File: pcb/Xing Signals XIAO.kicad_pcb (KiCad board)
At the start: 2 copper layers, 59.1 x 45.7 mm, 48 parts, among them J1 Barrel_Jack_Switch, J10 Signals, J2 DCC IN, J3 Signals, J4 Signal Gate 1, J5 Signal Gate 2, J6 Conn_01x07_Pin, J7 Sensor Power, J8 Screw_Terminal_01x04, J9 Conn_01x07_Pin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

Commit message: Version 1.1 of the PCB
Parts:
- removed J5: Signal Gate 2, Connector_PinHeader_2.54mm:PinHeader_1x03_P2.54mm_Vertical
- removed R16, R17: 100, Resistor_SMD:R_0402_1005Metric
- added R18: 100, Resistor_SMD:R_0402_1005Metric, F.Cu at (60.5, 63.2)
- added R19: 100, Resistor_SMD:R_0402_1005Metric, F.Cu at (60.5, 60.5)
- added R20: 100, Resistor_SMD:R_0402_1005Metric, F.Cu at (60.5, 68.3)
- J4: value Signal Gate 1 -> Conn_02x03_Top_Bottom; footprint Connector_PinHeader_2.54mm:PinHeader_1x03_P2.54mm_Vertical -> Connector_PinHeader_2.54mm:PinHeader_2x03_P2.54mm_Vertical
- R1: value 100ohm -> 100; footprint Resistor_SMD:R_1206_3216Metric -> Resistor_SMD:R_0402_1005Metric
- R2: value 100ohm -> 1k
- R3: value 200 -> 1k
- moved J7 14.8 mm to (64.5, 77.2)
- moved D7 9.70 mm to (84.1, 77.4), turned to -90 degrees
- moved R2 8.98 mm to (77.7, 62.2)
- moved J3 8.95 mm to (75.2, 77.2)
- moved D6 8.18 mm to (71.4, 77.4), turned to -90 degrees
- moved Q2 4.59 mm to (70.9, 68.2)
- moved R4 4.59 mm to (71.8, 64.8)
- moved BR1 4.38 mm to (86.4, 66.4)
- moved VIN 4.32 mm to (88.9, 57.9)
- moved C1 3.82 mm to (96.2, 58.9)
- moved GND 3.78 mm to (83.8, 57.9)
- moved Q3 3.34 mm to (74.7, 68.2)
- moved R1 3.31 mm to (60.5, 65.8), turned to 180 degrees
- moved R5 3.26 mm to (75.6, 64.8)
- moved J4 2.81 mm to (51.1, 49.3)
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- renumbered TP3 to +5V, TP1 to GND, TP2 to VIN
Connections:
- D1 pad 1: GND -> Net-(D1-K)
- D2 pad 1: GND -> Net-(D2-K)
- D3 pad 1: GND -> Net-(D3-K)
- D4 pad 1: GND -> Net-(D4-K)
- D6 pad 1: GND -> Net-(D6-K)
- D7 pad 1: GND -> Net-(D7-K)
- D7 pad 2: Net-(D7-A) -> Net-(D6-A)
- J3 pad 1: Net-(J3-Pin_1) -> Net-(D6-K)
- J3 pad 2: Net-(J3-Pin_2) -> Net-(D6-A)
- J3 pad 3: Net-(J3-Pin_3) -> Net-(D7-K)
- J4 pad 2: +3V3 -> GND
- J4 pad 3: GATE1 -> +3V3
- Q2 pad 2: Net-(Q2-E) -> GND
- Q2 pad 3: Net-(J3-Pin_1) -> Net-(D6-K)
- Q3 pad 2: Net-(Q3-E) -> GND
- Q3 pad 3: Net-(J3-Pin_3) -> Net-(D7-K)
- Q4 pad 3: Net-(Q4-C) -> +3V3
- Q5 pad 3: Net-(Q4-C) -> +3V3
- Q6 pad 3: Net-(Q4-C) -> +3V3
- Q7 pad 3: Net-(Q4-C) -> +3V3
- R1 pad 1: +3V3 -> GND
- R1 pad 2: Net-(Q4-C) -> Net-(D3-K)
- R2 pad 2: Net-(J3-Pin_2) -> Net-(D6-A)
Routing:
- net Net-(D6-A): track 1.80 -> 28.3 mm
- net Net-(Q4-C): track 20.8 -> 0.00 mm
- net Net-(D7-K): track 0.00 -> 15.8 mm, vias 0 -> 2
- net Net-(J3-Pin_2): track 14.1 -> 0.00 mm
- net Net-(D6-K): track 0.00 -> 14.0 mm
- net +3V3: track 115.3 -> 125.0 mm
- net Net-(Q3-E): track 9.72 -> 0.00 mm, vias 2 -> 0
- net Net-(J3-Pin_3): track 6.48 -> 0.00 mm
- net Net-(J3-Pin_1): track 6.48 -> 0.00 mm
- net Net-(Q2-E): track 6.13 -> 0.00 mm
- net Net-(U2-VI): track 38.9 -> 44.5 mm
- net SIGRIGHT: track 16.3 -> 12.7 mm
- net Net-(J2-Pin_2): track 19.8 -> 16.5 mm
- net Net-(BR1-~.): track 13.0 -> 10.4 mm
- net Net-(D7-A): track 1.82 -> 0.00 mm
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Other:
- board text added: "Crossing Gate Control Version 1.1 (C) Peter Buelow Februrary 2024"
- board text removed: "Crossing Gate Control Version 1.0 (C) Peter Buelow January 2024"

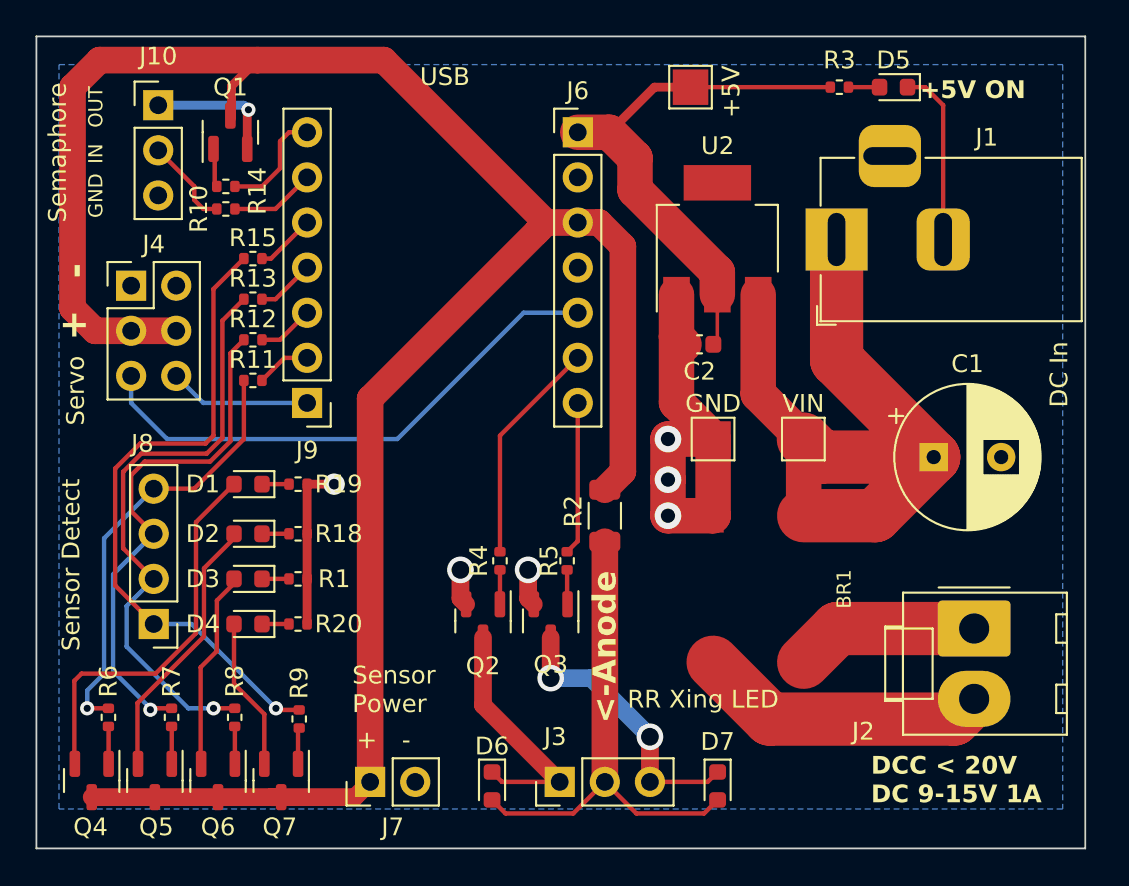
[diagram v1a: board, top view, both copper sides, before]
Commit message: Fixes to Version 1.1
* Trace fixups
* Components moved to better fit
* Move the sensor screw terminals next to each other
* Cleaned up the transistor layout for the sensor LED indicators
* Servo pins are now 2x3
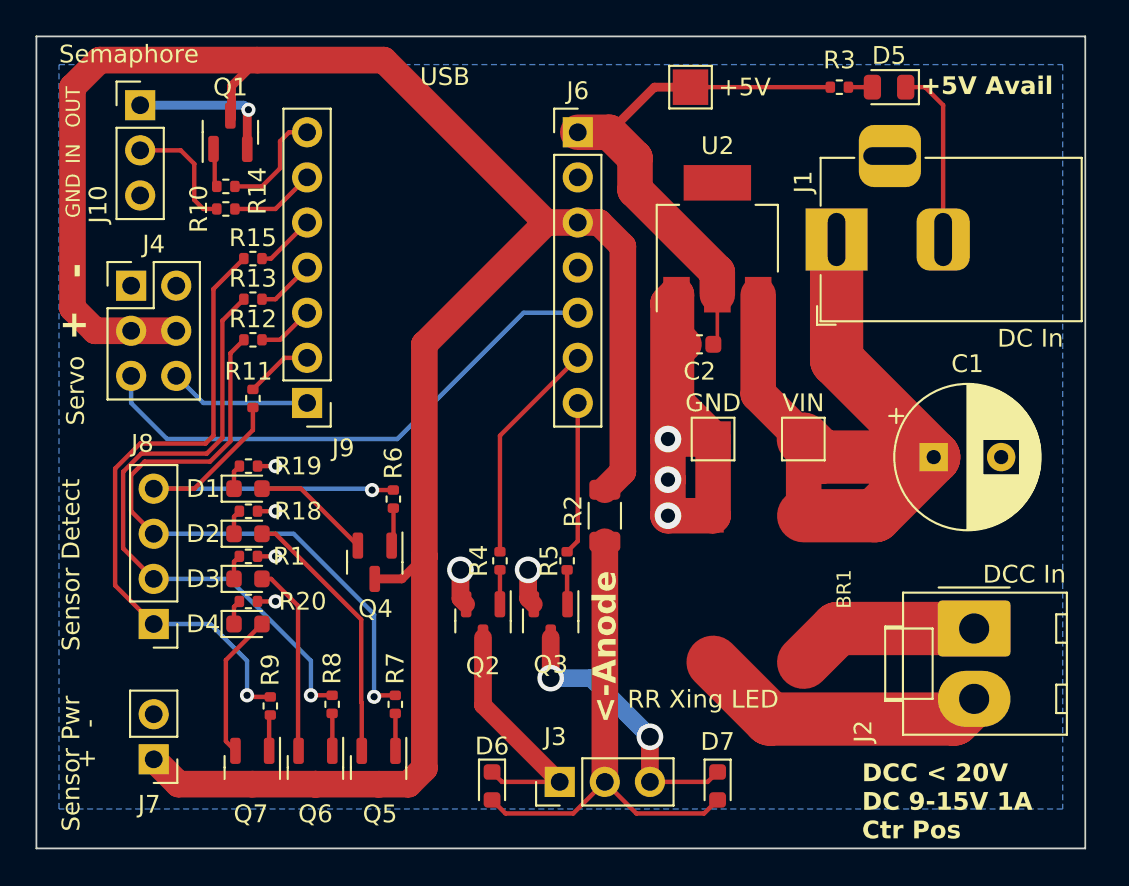
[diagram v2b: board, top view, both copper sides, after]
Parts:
- D5: value White -> Green; footprint LED_SMD:LED_0603_1608Metric -> LED_SMD:LED_0805_2012Metric
- J2: value DCC IN -> DCC In
- TP2: renamed from VIN; value +12V -> VIN
- moved R6 20.2 mm to (65.8, 61.3)
- moved Q4 20.1 mm to (64.8, 64.8)
- moved R7 12.6 mm to (65.9, 72.9)
- moved Q5 12.6 mm to (65.0, 76.4)
- moved J7 12.3 mm to (52.3, 75.9), turned to 180 degrees
- moved Q6 5.53 mm to (61.4, 76.4)
- moved R8 5.53 mm to (62.4, 72.8)
- moved R1 3.07 mm to (57.7, 64.5)
- moved R18 3.07 mm to (57.7, 62.0)
- moved R20 3.07 mm to (57.7, 67.1)
- moved R19 2.97 mm to (57.7, 59.4)
- moved Q7 1.78 mm to (57.9, 76.4)
- moved R9 1.78 mm to (58.9, 72.9)
- moved J10 1.02 mm to (51.6, 39.1)
- moved R11 1.02 mm to (57.9, 55.6), turned to 90 degrees
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- renumbered GND to TP1, +5V to TP3
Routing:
- net Net-(D1-A): track 21.9 -> 6.77 mm
- net DETECT2: track 29.1 -> 36.4 mm
- net GND: track 47.2 -> 50.3 mm, vias 6 -> 9
- net DETECT1: track 24.7 -> 21.7 mm
- net DETECT3: track 33.4 -> 35.3 mm
- net Net-(J10-Pin_2): track 5.11 -> 6.87 mm
- net Net-(J10-Pin_1): track 7.42 -> 8.44 mm
- net +3V3: track 125.0 -> 125.9 mm
- net DETECT4: track 36.8 -> 36.0 mm
- net Net-(J9-Pin_2): track 3.07 -> 3.79 mm
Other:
- board text added: "+5V Avail"
- board text added: "DCC < 20V DC 9-15V 1A Ctr Pos"
- board text added: "Sensor Pwr"
- board text removed: "+5V ON"
- board text removed: "DCC < 20V DC 9-15V 1A"
- board text removed: "Sensor Power"

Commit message: More fixes, ordered V1.1
* Added C3 to buffer the Servo current draw
* More fixes for traces
* Fixed TP2 to be VIN, not +12V
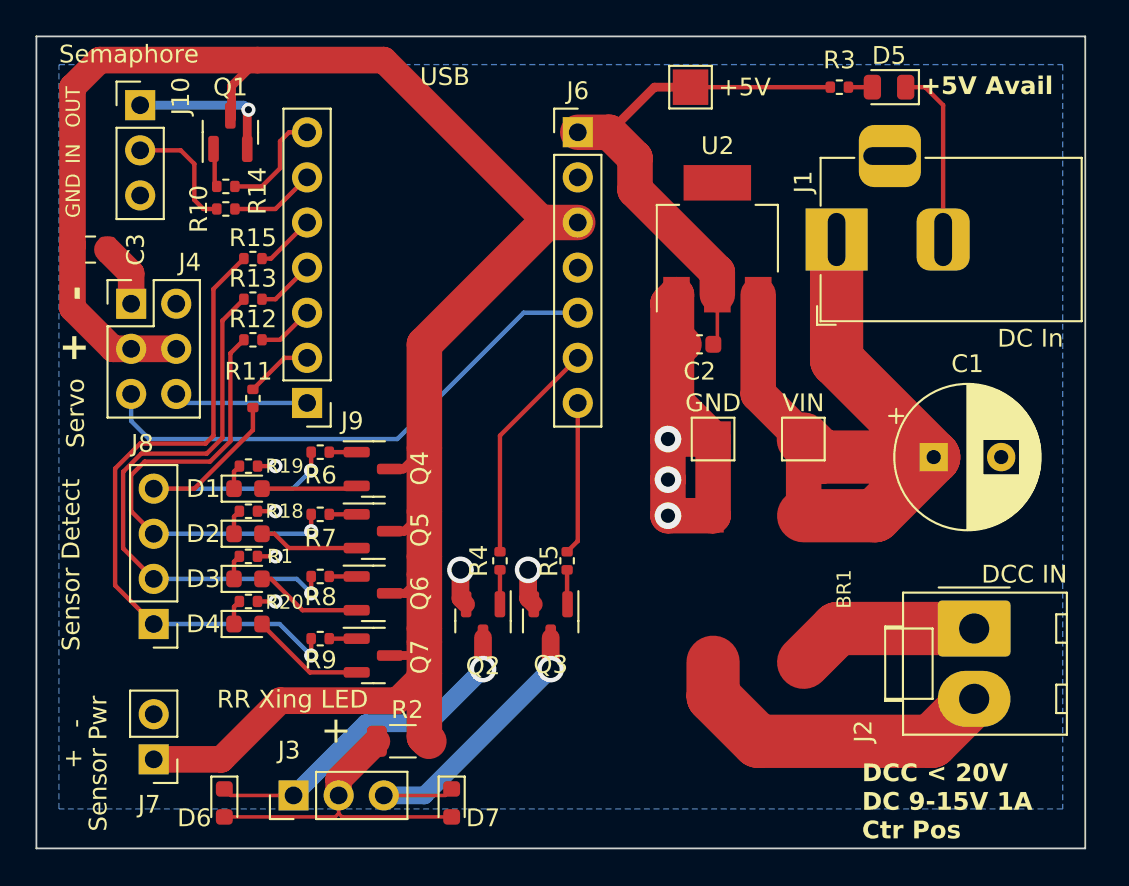
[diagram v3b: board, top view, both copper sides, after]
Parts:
- added C3: 47uf, Capacitor_SMD:C_0805_2012Metric, F.Cu at (48.8, 47.2)
- J2: value DCC In -> DCC IN
- moved R2 17.0 mm to (66.4, 74.9), turned to 180 degrees
- moved D6 15.1 mm to (56.3, 78.4)
- moved J3 15.0 mm to (60.2, 78.0)
- moved D7 15.0 mm to (69.1, 78.4)
- moved Q5 13.3 mm to (64.7, 63.1), turned to 0 degrees
- moved R7 11.5 mm to (61.7, 62.1), turned to 0 degrees
- moved Q6 10.3 mm to (64.7, 66.6), turned to 0 degrees
- moved Q7 9.28 mm to (64.7, 70.1), turned to 0 degrees
- moved R8 7.23 mm to (61.7, 65.7), turned to 180 degrees
- moved Q4 5.25 mm to (64.7, 59.6), turned to 0 degrees
- moved R6 4.89 mm to (61.7, 58.6), turned to 180 degrees
- moved R9 4.72 mm to (61.7, 69.2), turned to 180 degrees
- moved J4 1.02 mm to (51.1, 50.3)
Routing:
- net +3V3: track 125.9 -> 114.9 mm
- net Net-(D6-A): track 28.3 -> 17.9 mm
- net DETECT2: track 36.4 -> 26.1 mm
- net Net-(D2-A): track 15.0 -> 5.67 mm
- net Net-(D6-K): track 14.0 -> 19.4 mm, vias 0 -> 1
- net Net-(D3-A): track 10.8 -> 6.06 mm
- net DETECT3: track 35.3 -> 31.6 mm
- net GND: track 50.3 -> 53.9 mm
- net DETECT1: track 21.7 -> 18.5 mm
- net Net-(D7-K): track 15.8 -> 18.1 mm, vias 2 -> 1
- net Net-(J2-Pin_2): track 16.5 -> 18.7 mm
- net Net-(D4-A): track 8.21 -> 6.48 mm
- net Net-(D1-A): track 6.77 -> 5.40 mm
- net DETECT4: track 36.0 -> 37.2 mm
- net Net-(Q4-B): track 2.11 -> 1.54 mm
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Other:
- board text removed: "<-Anode"

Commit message: Version 1.2
* Fixed a clearance issue between J3 and C2
* Moved D6 and D7 a bit closer to J3
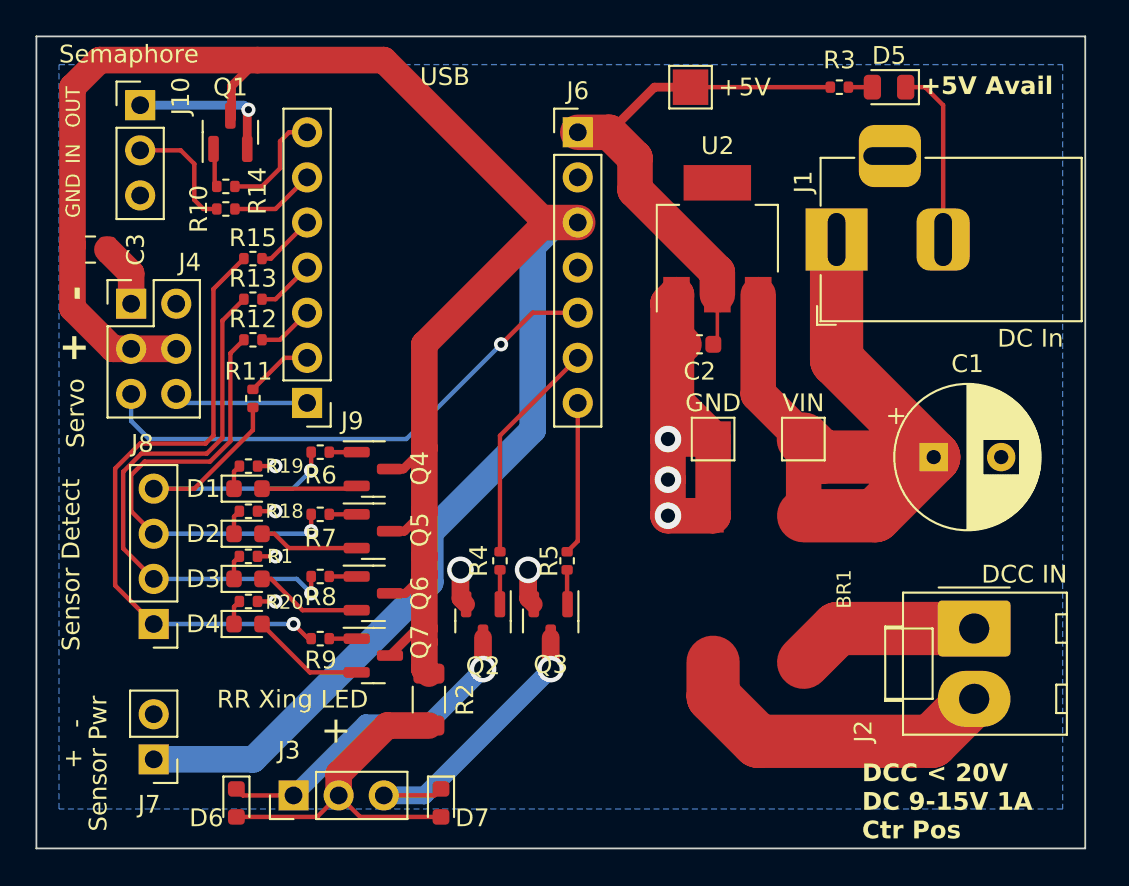
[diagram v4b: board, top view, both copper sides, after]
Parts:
- moved R2 2.77 mm to (67.8, 72.6), turned to -90 degrees
- moved D6 0.68 mm to (57.0, 78.4)
- moved D7 0.60 mm to (68.5, 78.4)
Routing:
- net +3V3: track 114.9 -> 138.2 mm
- net Net-(D6-A): track 17.9 -> 19.9 mm
- net DETECT4: track 37.2 -> 35.8 mm
- net Net-(D6-K): track 19.4 -> 18.8 mm
- net Net-(D7-K): track 18.1 -> 17.5 mm
- net GATE2: vias 0 -> 1
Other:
- board text added: "Crossing Gate Control Version 1.2 (C) Peter Buelow February 2024"
- board text removed: "Crossing Gate Control Version 1.1 (C) Peter Buelow Februrary 2024"
